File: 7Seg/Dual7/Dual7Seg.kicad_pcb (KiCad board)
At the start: 2 copper layers, 53.3 x 50.8 mm, 21 parts, among them J1 Conn_01x08, J2 Conn_01x08, J3 Conn_01x01, U1 D168K, U2 D168K

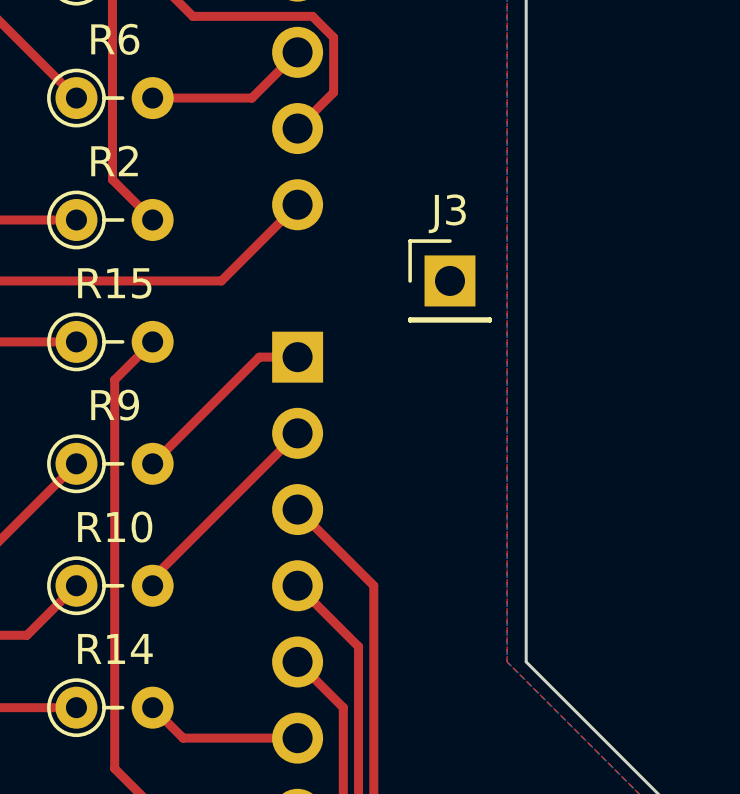
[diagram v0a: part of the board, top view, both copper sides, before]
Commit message: renamed components
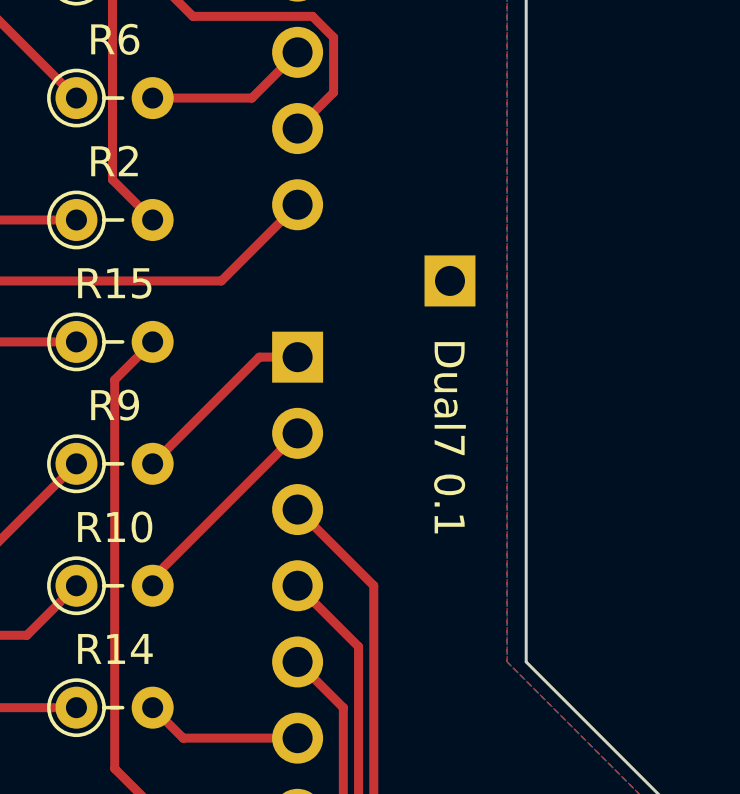
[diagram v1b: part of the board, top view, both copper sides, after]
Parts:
- J3: moved to B.Cu
- turned J3 to 180 degrees
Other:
- board text added: "Dual7 0.1"
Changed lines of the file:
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@@
-    )
-  )
-  (footprint "Connector_PinHeader_2.54mm:PinHeader_1x01_P2.54mm_Vertical" (layer "F.Cu")
-    (at 162.56 96.52)
-    (descr "Through hole straight pin header, 1x01, 2.54mm pitch, single row")
-    (tags "Through hole pin header THT 1x01 2.54mm single row")
-    (property "Sheetfile" "Double7Segment.kicad_sch")
-    (property "Sheetname" "")
-    (property "ki_description" "Generic connector, single row, 01x01, script generated (kicad-library-utils/schlib/autogen/connector/)")
-    (property "ki_keywords" "connector")
-    (attr through_hole)
-    (fp_text reference "J3" (at 0 -2.33) (layer "F.SilkS")
-        (effects (font (size 1 1) (thickness 0.15)))
-    )
-    (fp_text value "Conn_01x01" (at 0 2.33) (layer "F.Fab")
-        (effects (font (size 1 1) (thickness 0.15)))
-    )
-    (fp_text user "${REFERENCE}" (at 0 0 90) (layer "F.Fab")
-        (effects (font (size 1 1) (thickness 0.15)))
-    )
-    (fp_line (start -1.33 -1.33) (end 0 -1.33)
-      (stroke (width 0.12) (type solid)) (layer "F.SilkS"))
-    (fp_line (start -1.33 0) (end -1.33 -1.33)
-      (stroke (width 0.12) (type solid)) (layer "F.SilkS"))
-    (fp_line (start -1.33 1.27) (end -1.33 1.33)
-      (stroke (width 0.12) (type solid)) (layer "F.SilkS"))
-    (fp_line (start -1.33 1.27) (end 1.33 1.27)
-      (stroke (width 0.12) (type solid)) (layer "F.SilkS"))
-    (fp_line (start -1.33 1.33) (end 1.33 1.33)
-      (stroke (width 0.12) (type solid)) (layer "F.SilkS"))
-    (fp_line (start 1.33 1.27) (end 1.33 1.33)
-      (stroke (width 0.12) (type solid)) (layer "F.SilkS"))
-    (fp_line (start -1.8 -1.8) (end -1.8 1.8)
-      (stroke (width 0.05) (type solid)) (layer "F.CrtYd"))
-    (fp_line (start -1.8 1.8) (end 1.8 1.8)
-      (stroke (width 0.05) (type solid)) (layer "F.CrtYd"))
-    (fp_line (start 1.8 -1.8) (end -1.8 -1.8)
-      (stroke (width 0.05) (type solid)) (layer "F.CrtYd"))
-    (fp_line (start 1.8 1.8) (end 1.8 -1.8)
-      (stroke (width 0.05) (type solid)) (layer "F.CrtYd"))
-    (fp_line (start -1.27 -0.635) (end -0.635 -1.27)
-      (stroke (width 0.1) (type solid)) (layer "F.Fab"))
-    (fp_line (start -1.27 1.27) (end -1.27 -0.635)
-      (stroke (width 0.1) (type solid)) (layer "F.Fab"))
-    (fp_line (start -0.635 -1.27) (end 1.27 -1.27)
-      (stroke (width 0.1) (type solid)) (layer "F.Fab"))
-    (fp_line (start 1.27 -1.27) (end 1.27 1.27)
-      (stroke (width 0.1) (type solid)) (layer "F.Fab"))
-    (fp_line (start 1.27 1.27) (end -1.27 1.27)
-      (stroke (width 0.1) (type solid)) (layer "F.Fab"))
-    (pad "1" thru_hole rect (at 0 0) (size 1.7 1.7) (drill 1) (layers "*.Cu" "*.Mask")
-      (net 3 "GND") (pinfunction "Pin_1") (pintype "passive"))
-    (model "${KICAD6_3DMODEL_DIR}/Connector_PinHeader_2.54mm.3dshapes/PinHeader_1x01_P2.54mm_Vertical.wrl"
-      (offset (xyz 0 0 0))
-      (scale (xyz 1 1 1))
-      (rotate (xyz 0 0 0))
     )
   )
@@
     )
   )
+  (footprint "Connector_PinHeader_2.54mm:PinHeader_1x01_P2.54mm_Vertical" (layer "B.Cu")
+    (at 162.56 96.52 180)
+    (descr "Through hole straight pin header, 1x01, 2.54mm pitch, single row")
+    (tags "Through hole pin header THT 1x01 2.54mm single row")
+    (property "Sheetfile" "Double7Segment.kicad_sch")
+    (property "Sheetname" "")
+    (property "ki_description" "Generic connector, single row, 01x01, script generated (kicad-library-utils/schlib/autogen/connector/)")
+    (property "ki_keywords" "connector")
+    (attr through_hole)
+    (fp_text reference "J3" (at 0 2.33) (layer "B.SilkS")
+        (effects (font (size 1 1) (thickness 0.15)) (justify mirror))
+    )
+    (fp_text value "Conn_01x01" (at 0 -2.33) (layer "B.Fab")
+        (effects (font (size 1 1) (thickness 0.15)) (justify mirror))
+    )
+    (fp_text user "${REFERENCE}" (at 0 0 90) (layer "B.Fab")
+        (effects (font (size 1 1) (thickness 0.15)) (justify mirror))
+    )
+    (fp_line (start -1.33 -1.33) (end 1.33 -1.33)
+      (stroke (width 0.12) (type solid)) (layer "B.SilkS"))
+    (fp_line (start -1.33 -1.27) (end -1.33 -1.33)
+      (stroke (width 0.12) (type solid)) (layer "B.SilkS"))
+    (fp_line (start -1.33 -1.27) (end 1.33 -1.27)
+      (stroke (width 0.12) (type solid)) (layer "B.SilkS"))
+    (fp_line (start -1.33 0) (end -1.33 1.33)
+      (stroke (width 0.12) (type solid)) (layer "B.SilkS"))
+    (fp_line (start -1.33 1.33) (end 0 1.33)
+      (stroke (width 0.12) (type solid)) (layer "B.SilkS"))
+    (fp_line (start 1.33 -1.27) (end 1.33 -1.33)
+      (stroke (width 0.12) (type solid)) (layer "B.SilkS"))
+    (fp_line (start -1.8 -1.8) (end 1.8 -1.8)
+      (stroke (width 0.05) (type solid)) (layer "B.CrtYd"))
+    (fp_line (start -1.8 1.8) (end -1.8 -1.8)
+      (stroke (width 0.05) (type solid)) (layer "B.CrtYd"))
+    (fp_line (start 1.8 -1.8) (end 1.8 1.8)
+      (stroke (width 0.05) (type solid)) (layer "B.CrtYd"))
+    (fp_line (start 1.8 1.8) (end -1.8 1.8)
+      (stroke (width 0.05) (type solid)) (layer "B.CrtYd"))
+    (fp_line (start -1.27 -1.27) (end -1.27 0.635)
+      (stroke (width 0.1) (type solid)) (layer "B.Fab"))
+    (fp_line (start -1.27 0.635) (end -0.635 1.27)
+      (stroke (width 0.1) (type solid)) (layer "B.Fab"))
+    (fp_line (start -0.635 1.27) (end 1.27 1.27)
+      (stroke (width 0.1) (type solid)) (layer "B.Fab"))
+    (fp_line (start 1.27 -1.27) (end -1.27 -1.27)
+      (stroke (width 0.1) (type solid)) (layer "B.Fab"))
+    (fp_line (start 1.27 1.27) (end 1.27 -1.27)
+      (stroke (width 0.1) (type solid)) (layer "B.Fab"))
+    (pad "1" thru_hole rect (at 0 0 180) (size 1.7 1.7) (drill 1) (layers "*.Cu" "*.Mask")
+      (net 3 "GND") (pinfunction "Pin_1") (pintype "passive"))
+    (model "${KICAD6_3DMODEL_DIR}/Connector_PinHeader_2.54mm.3dshapes/PinHeader_1x01_P2.54mm_Vertical.wrl"
+      (offset (xyz 0 0 0))
+      (scale (xyz 1 1 1))
+      (rotate (xyz 0 0 0))
+    )
+  )
   (footprint "Connector_PinHeader_2.54mm:PinHeader_1x08_P2.54mm_Vertical" (layer "B.Cu")
     (at 157.48 76.2 180)
@@
   (gr_line (start 170.18 73.66) (end 170.18 78.74)
     (stroke (width 0.1) (type default)) (layer "Edge.Cuts"))
+  (gr_text "Dual7 0.1" (at 161.925 98.425 -90) (layer "F.SilkS")
+    (effects (font (size 1 1) (thickness 0.15)) (justify left bottom))
+  )
   (segment (start 135.379 72.652) (end 130.556 77.475) (width 0.3) (layer "F.Cu") (net 1))
   (segment (start 157.48 86.36) (end 160.18 83.66) (width 0.3) (layer "F.Cu") (net 1))

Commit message: updated bitshift, dual7 and dualbitshift
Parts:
- moved R1 5.08 mm to (150.1, 77.2)
- moved R10 5.08 mm to (150.1, 101.6)
- moved R11 5.08 mm to (134.6, 107.9)
- moved R12 5.08 mm to (138.7, 107.9)
- moved R13 5.08 mm to (142.7, 107.9)
- moved R15 5.08 mm to (150.1, 93.5)
- moved R16 5.08 mm to (130.6, 107.9)
- moved R6 5.08 mm to (150.1, 85.3)
- moved U2 5.08 mm to (129.7, 93.1)
- moved J1 5.08 mm to (157.5, 71.1)
- moved J2 5.08 mm to (157.5, 94.0)
- moved J3 5.08 mm to (162.6, 91.4)
- moved R14 5.08 mm to (150.1, 105.7)
- moved R2 5.08 mm to (150.1, 89.4)
- moved R3 5.08 mm to (138.7, 74.9)
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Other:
- board size 53.3 x 50.8 mm -> 53.3 x 61 mm
- board text added: "1"
- board text added: "10"
- board text added: "11"
- board text added: "12"
- board text added: "13"
- board text added: "14"
- board text added: "15"
- board text added: "16"
- board text added: "2"
- board text added: "3"
- board text added: "4"
- board text added: "5"
- board text added: "6"
- board text added: "7"
- board text added: "8"
- board text added: "9"
- board text added: "Dual7 0.2"
- board text removed: "Dual7 0.1"
